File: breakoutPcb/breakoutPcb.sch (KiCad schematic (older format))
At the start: 16 parts, among them J1 DB9_Female_MountingHoles, J2 ConY1, J3 ConY2, J4 ConX1, J5 ConX2

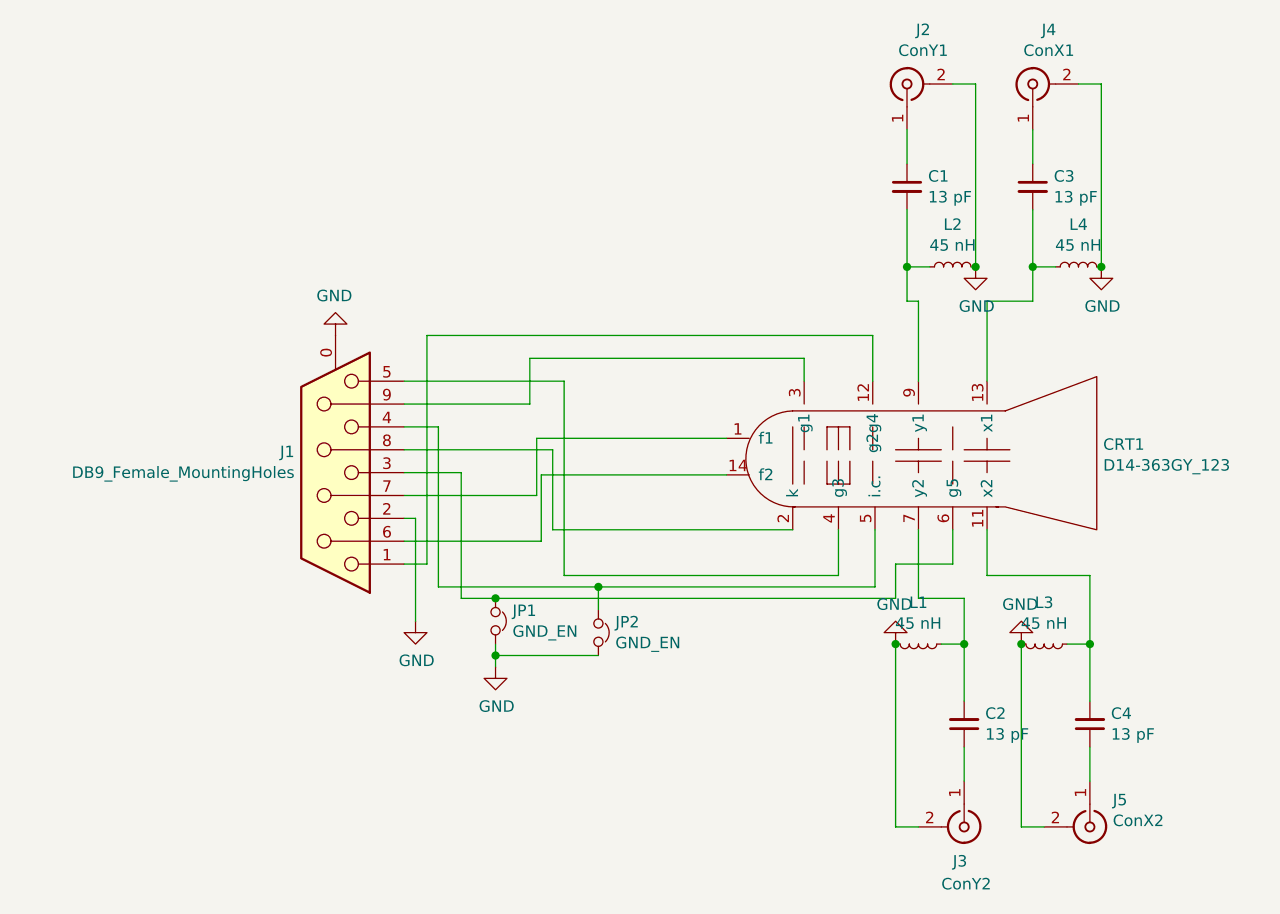
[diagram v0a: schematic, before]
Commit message: Matching adapted to reality
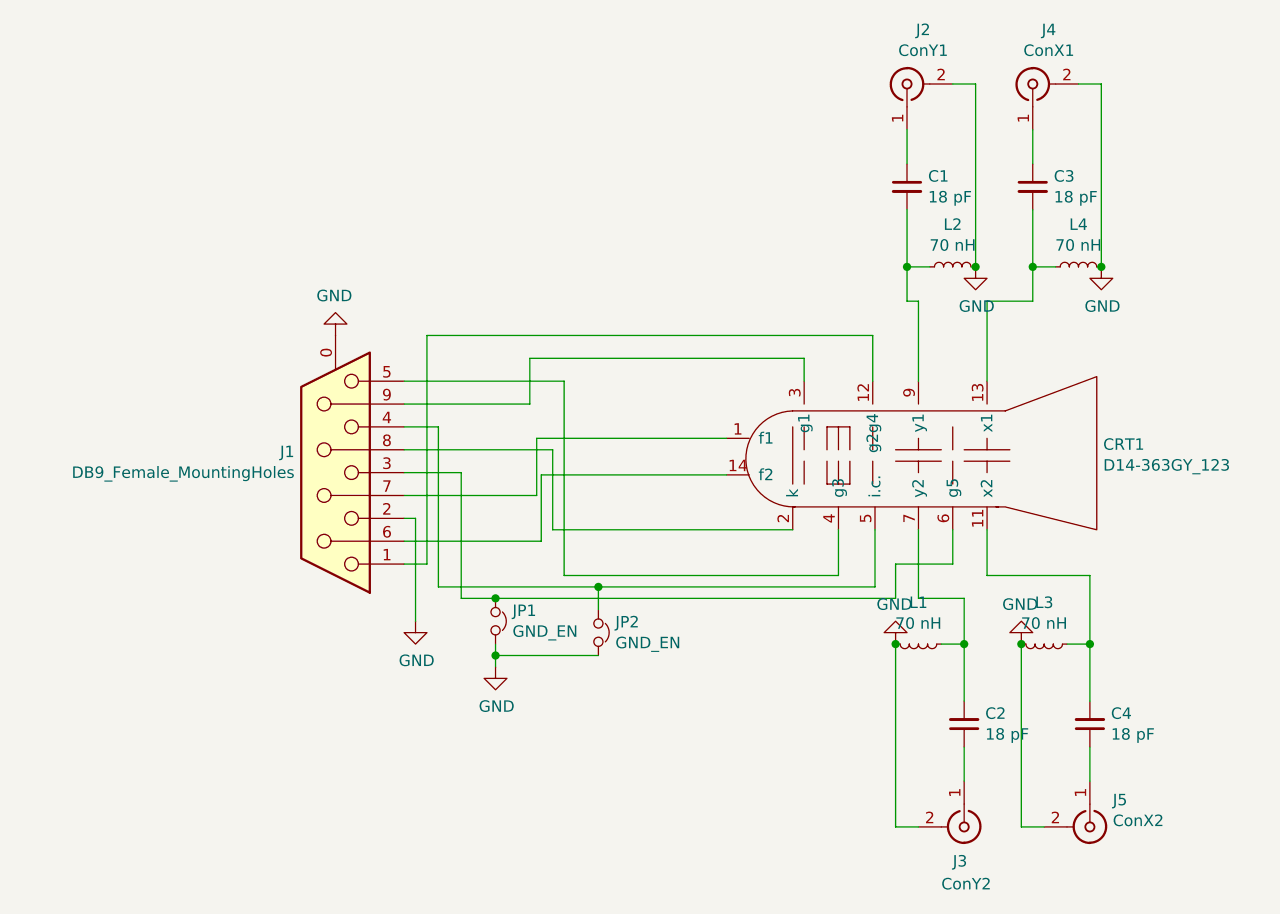
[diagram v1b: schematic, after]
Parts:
- C1, C2, C3, C4: value 13 pF -> 18 pF
- L1, L2, L3, L4: value 45 nH -> 70 nH; footprint Inductor_SMD:L_1008_2520Metric -> Wurth:Wurth4035
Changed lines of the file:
@@
 P 5650 1750
 F 0 "C1" H 5742 1796 50  0000 L CNN
-F 1 "13 pF" H 5742 1705 50  0000 L CNN
+F 1 "18 pF" H 5742 1705 50  0000 L CNN
 F 2 "Capacitor_SMD:C_0201_0603Metric" H 5650 1750 50  0001 C CNN
 F 3 "~" H 5650 1750 50  0001 C CNN
@@
 P 5850 2100
 F 0 "L2" V 6035 2100 50  0000 C CNN
-F 1 "45 nH" V 5944 2100 50  0000 C CNN
-F 2 "Inductor_SMD:L_1008_2520Metric" H 5850 2100 50  0001 C CNN
+F 1 "70 nH" V 5944 2100 50  0000 C CNN
+F 2 "Wurth:Wurth4035" H 5850 2100 50  0001 C CNN
 F 3 "~" H 5850 2100 50  0001 C CNN
 	1    5850 2100
@@
 P 6200 1750
 F 0 "C3" H 6292 1796 50  0000 L CNN
-F 1 "13 pF" H 6292 1705 50  0000 L CNN
+F 1 "18 pF" H 6292 1705 50  0000 L CNN
 F 2 "Capacitor_SMD:C_0201_0603Metric" H 6200 1750 50  0001 C CNN
 F 3 "~" H 6200 1750 50  0001 C CNN
@@
 P 6400 2100
 F 0 "L4" V 6585 2100 50  0000 C CNN
-F 1 "45 nH" V 6494 2100 50  0000 C CNN
-F 2 "Inductor_SMD:L_1008_2520Metric" H 6400 2100 50  0001 C CNN
+F 1 "70 nH" V 6494 2100 50  0000 C CNN
+F 2 "Wurth:Wurth4035" H 6400 2100 50  0001 C CNN
 F 3 "~" H 6400 2100 50  0001 C CNN
 	1    6400 2100
@@
 P 6450 4100
 F 0 "C4" H 6358 4054 50  0000 R CNN
-F 1 "13 pF" H 6358 4145 50  0000 R CNN
+F 1 "18 pF" H 6358 4145 50  0000 R CNN
 F 2 "Capacitor_SMD:C_0201_0603Metric" H 6450 4100 50  0001 C CNN
 F 3 "~" H 6450 4100 50  0001 C CNN
@@
 P 6250 3750
 F 0 "L3" V 6069 3750 50  0000 C CNN
-F 1 "45 nH" V 6160 3750 50  0000 C CNN
-F 2 "Inductor_SMD:L_1008_2520Metric" H 6250 3750 50  0001 C CNN
+F 1 "70 nH" V 6160 3750 50  0000 C CNN
+F 2 "Wurth:Wurth4035" H 6250 3750 50  0001 C CNN
 F 3 "~" H 6250 3750 50  0001 C CNN
 	1    6250 3750
@@
 P 5900 4100
 F 0 "C2" H 5808 4054 50  0000 R CNN
-F 1 "13 pF" H 5808 4145 50  0000 R CNN
+F 1 "18 pF" H 5808 4145 50  0000 R CNN
 F 2 "Capacitor_SMD:C_0201_0603Metric" H 5900 4100 50  0001 C CNN
 F 3 "~" H 5900 4100 50  0001 C CNN
@@
 P 5700 3750
 F 0 "L1" V 5519 3750 50  0000 C CNN
-F 1 "45 nH" V 5610 3750 50  0000 C CNN
-F 2 "Inductor_SMD:L_1008_2520Metric" H 5700 3750 50  0001 C CNN
+F 1 "70 nH" V 5610 3750 50  0000 C CNN
+F 2 "Wurth:Wurth4035" H 5700 3750 50  0001 C CNN
 F 3 "~" H 5700 3750 50  0001 C CNN
 	1    5700 3750
@@
 	3550 3400 3450 3400
 $Comp
-L power:GND #PWR?
+L power:GND #PWR0106
 U 1 1 6254D1E8
 P 3500 3650
-F 0 "#PWR?" H 3500 3400 50  0001 C CNN
+F 0 "#PWR0106" H 3500 3400 50  0001 C CNN
 F 1 "GND" H 3505 3477 50  0000 C CNN
 F 2 "" H 3500 3650 50  0001 C CNN

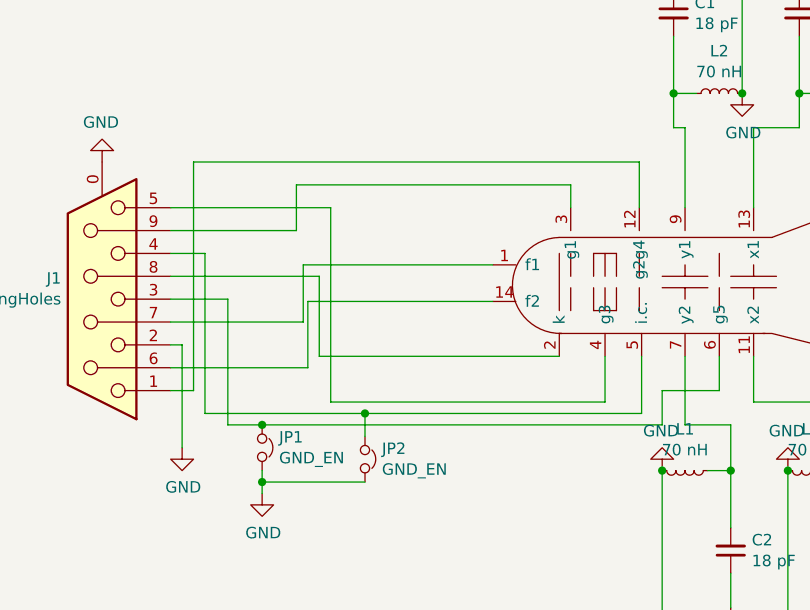
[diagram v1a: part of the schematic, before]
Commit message: Symmetrized layout, changed connector assignment
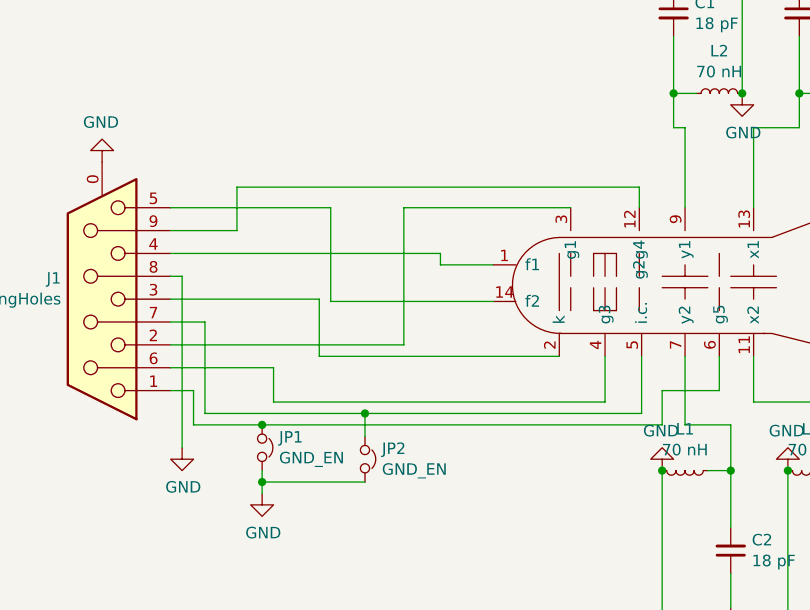
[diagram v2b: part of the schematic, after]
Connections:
- net GND: now also J1.8; no longer J1.2
- net at CRT1.1 (f1): now also J1.4; no longer J1.7
- net at CRT1.12 (g2g4): now also J1.9; no longer J1.1
- net at CRT1.14 (f2): now also J1.5; no longer J1.6
- net at CRT1.2 (k): now also J1.3; no longer J1.8
- net at CRT1.3 (g1): now also J1.2; no longer J1.9
- net at CRT1.4 (g3): now also J1.6; no longer J1.5
- net at CRT1.5 (i.c.), JP2.1: now also J1.7; no longer J1.4
- net at CRT1.6 (g5), JP1.1: now also J1.1; no longer J1.3
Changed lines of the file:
@@
 	5350 3450 5350 3250
 Wire Wire Line
-	5200 2500 5200 2600
-Wire Wire Line
 	5510 3500 5510 3250
-Wire Wire Line
-	5500 2400 5500 2600
 Wire Wire Line
 	3850 3550 5600 3550
@@
 $EndComp
 Wire Wire Line
-	4860 2850 4030 2850
-Wire Wire Line
-	4030 2850 4030 3100
-Wire Wire Line
-	4030 3100 3450 3100
-Wire Wire Line
-	4860 3010 4050 3010
-Wire Wire Line
-	4050 3010 4050 3300
-Wire Wire Line
-	4050 3300 3450 3300
-Wire Wire Line
-	5150 3250 4100 3250
-Wire Wire Line
-	4100 3250 4100 2900
-Wire Wire Line
-	4100 2900 3450 2900
-Wire Wire Line
-	5200 2500 4000 2500
-Wire Wire Line
-	4000 2500 4000 2700
-Wire Wire Line
-	4000 2700 3450 2700
-Wire Wire Line
-	5350 3450 4150 3450
-Wire Wire Line
-	4150 3450 4150 2600
-Wire Wire Line
-	4150 2600 3450 2600
-Wire Wire Line
 	4300 3500 3600 3500
-Wire Wire Line
-	3600 3500 3600 2800
-Wire Wire Line
-	3600 2800 3450 2800
 Connection ~ 4300 3500
-Wire Wire Line
-	3850 3550 3700 3550
-Wire Wire Line
-	3700 3550 3700 3000
-Wire Wire Line
-	3700 3000 3450 3000
 Connection ~ 3850 3550
-Wire Wire Line
-	5500 2400 3550 2400
-Wire Wire Line
-	3550 2400 3550 3400
-Wire Wire Line
-	3550 3400 3450 3400
 $Comp
 L power:GND #PWR0106
@@
 $EndComp
 Wire Wire Line
-	3450 3200 3500 3200
+	4860 3010 4150 3010
 Wire Wire Line
-	3500 3200 3500 3650
+	4150 3010 4150 2600
+Wire Wire Line
+	4150 2600 3450 2600
+Wire Wire Line
+	3450 2800 4630 2800
+Wire Wire Line
+	4630 2800 4630 2850
+Wire Wire Line
+	4630 2850 4860 2850
+Wire Wire Line
+	5150 3250 4100 3250
+Wire Wire Line
+	4100 3250 4100 3000
+Wire Wire Line
+	4100 3000 3450 3000
+Wire Wire Line
+	5200 2600 4470 2600
+Wire Wire Line
+	4470 2600 4470 3200
+Wire Wire Line
+	4470 3200 3450 3200
+Wire Wire Line
+	3550 3550 3550 3400
+Wire Wire Line
+	3550 3400 3450 3400
+Wire Wire Line
+	3550 3550 3850 3550
+Wire Wire Line
+	5500 2600 5500 2510
+Wire Wire Line
+	5500 2510 3740 2510
+Wire Wire Line
+	3740 2510 3740 2700
+Wire Wire Line
+	3740 2700 3450 2700
+Wire Wire Line
+	3600 3500 3600 3100
+Wire Wire Line
+	3600 3100 3450 3100
+Wire Wire Line
+	3900 3450 3900 3300
+Wire Wire Line
+	3900 3300 3450 3300
+Wire Wire Line
+	3900 3450 5350 3450
+Wire Wire Line
+	3500 3650 3500 2900
+Wire Wire Line
+	3500 2900 3450 2900
 $EndSCHEMATC
